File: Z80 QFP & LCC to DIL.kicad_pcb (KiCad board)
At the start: 2 copper layers, 25.4 x 101.6 mm, 3 parts, among them IC1 Z80CPU-LCC, IC2 Z80CPU-LQFP, IC3 Z80CPU-DIP

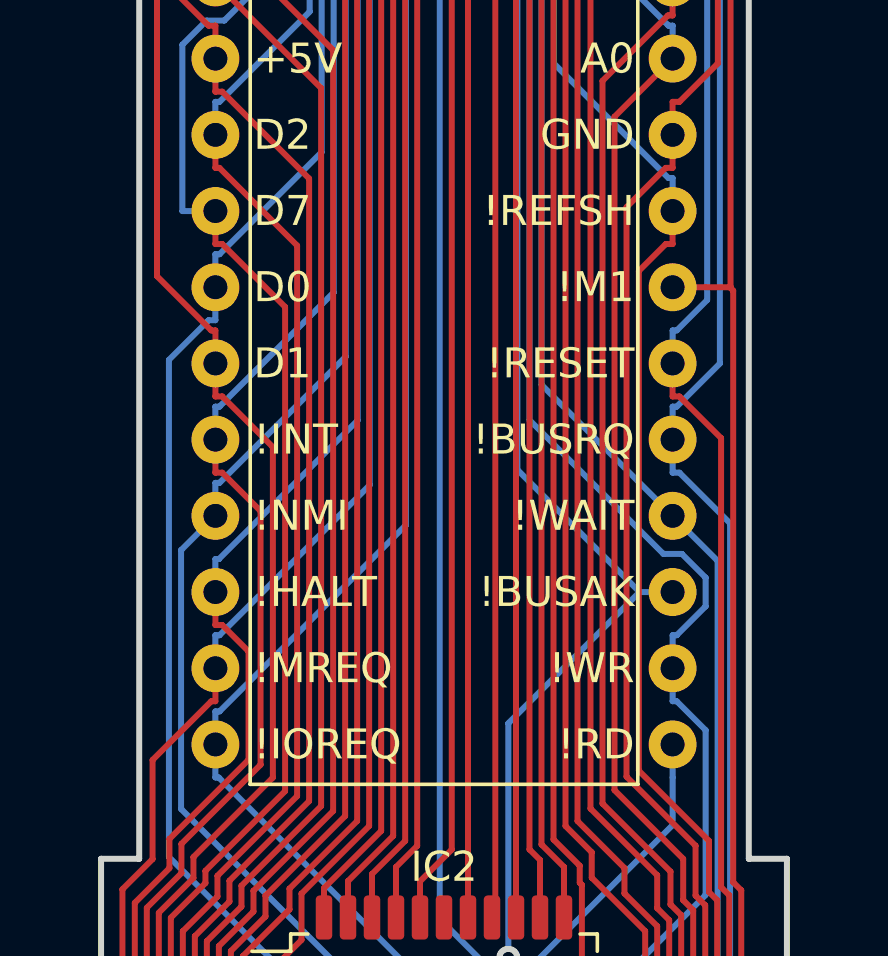
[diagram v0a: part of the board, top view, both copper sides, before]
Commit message: Change text for inveted logic pins from ! to ~{}
Signed-off-by: John Bradley <flypie@rocketmail.com>
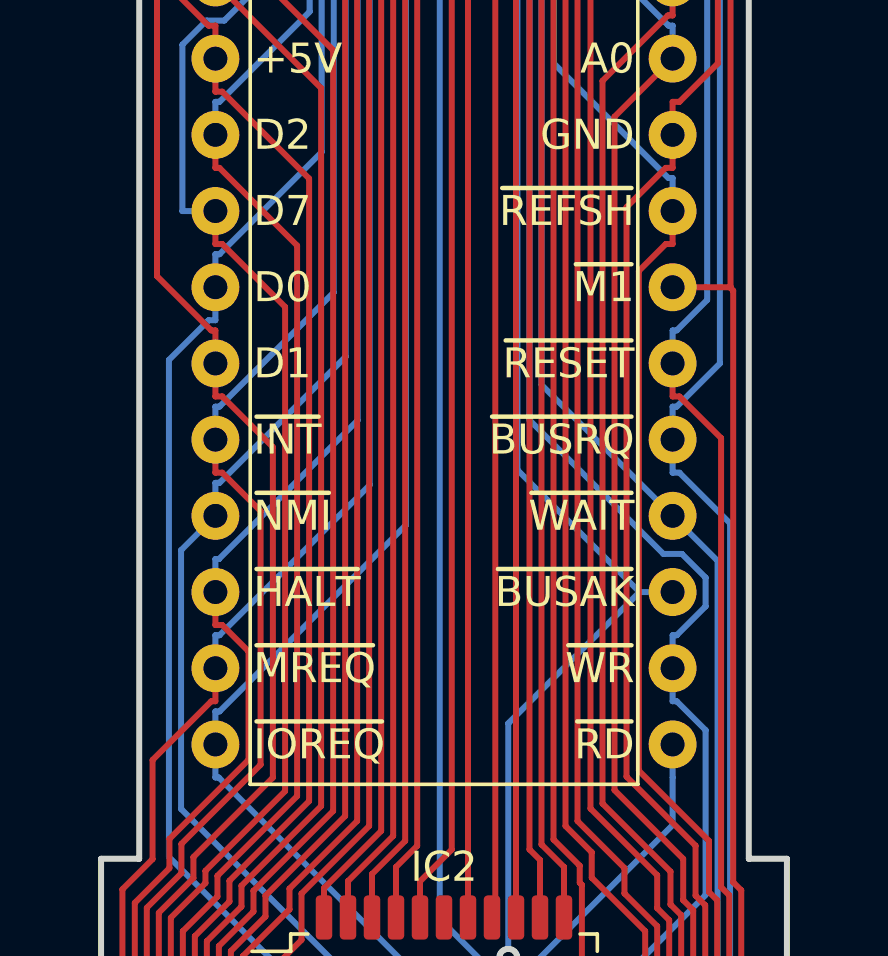
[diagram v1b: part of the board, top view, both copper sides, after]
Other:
- board text added: "~{BUSAK}"
- board text added: "~{BUSRQ}"
- board text added: "~{HALT}"
- board text added: "~{INT}"
- board text added: "~{IOREQ}"
- board text added: "~{M1}"
- board text added: "~{MREQ}"
- board text added: "~{NMI}"
- board text added: "~{RD}"
- board text added: "~{REFSH}"
- board text added: "~{RESET}"
- board text added: "~{WAIT}"
- board text added: "~{WR}"
- board text removed: "!BUSAK"
- board text removed: "!BUSRQ"
- board text removed: "!HALT"
- board text removed: "!INT"
- board text removed: "!IOREQ"
- board text removed: "!M1"
- board text removed: "!MREQ"
- board text removed: "!NMI"
- board text removed: "!RD"
- board text removed: "!REFSH"
- board text removed: "!RESET"
- board text removed: "!WAIT"
- board text removed: "!WR"
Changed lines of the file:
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@@
     (effects (font (size 1 1) (thickness 0.15)) (justify left))
   )
-  (gr_text "!WAIT" (at 147.32 135.89) (layer "F.SilkS")
+  (gr_text "~{WAIT}" (at 147.32 135.89) (layer "F.SilkS")
     (effects (font (size 1 1) (thickness 0.15)) (justify right))
   )
-  (gr_text "!BUSRQ" (at 147.32 133.35) (layer "F.SilkS")
+  (gr_text "~{BUSRQ}" (at 147.32 133.35) (layer "F.SilkS")
     (effects (font (size 1 1) (thickness 0.15)) (justify right))
   )
-  (gr_text "!MREQ" (at 134.62 140.97) (layer "F.SilkS")
+  (gr_text "~{MREQ}" (at 134.62 140.97) (layer "F.SilkS")
     (effects (font (size 1 1) (thickness 0.15)) (justify left))
   )
@@
     (effects (font (size 1 1) (thickness 0.15)) (justify right))
   )
-  (gr_text "!RESET" (at 147.32 130.81) (layer "F.SilkS")
+  (gr_text "~{RESET}" (at 147.32 130.81) (layer "F.SilkS")
     (effects (font (size 1 1) (thickness 0.15)) (justify right))
   )
-  (gr_text "!M1" (at 147.32 128.27) (layer "F.SilkS")
+  (gr_text "~{M1}" (at 147.32 128.27) (layer "F.SilkS")
     (effects (font (size 1 1) (thickness 0.15)) (justify right))
   )
@@
     (effects (font (size 1 1) (thickness 0.15)) (justify left))
   )
-  (gr_text "!REFSH" (at 147.32 125.73) (layer "F.SilkS")
+  (gr_text "~{REFSH}" (at 147.32 125.73) (layer "F.SilkS")
     (effects (font (size 1 1) (thickness 0.15)) (justify right))
   )
@@
     (effects (font (size 1 1) (thickness 0.15)) (justify left))
   )
-  (gr_text "!INT" (at 134.62 133.35) (layer "F.SilkS")
+  (gr_text "~{INT}" (at 134.62 133.35) (layer "F.SilkS")
     (effects (font (size 1 1) (thickness 0.15)) (justify left))
   )
@@
     (effects (font (size 1 1) (thickness 0.15)) (justify right))
   )
-  (gr_text "!BUSAK" (at 147.32 138.43) (layer "F.SilkS")
+  (gr_text "~{BUSAK}" (at 147.32 138.43) (layer "F.SilkS")
     (effects (font (size 1 1) (thickness 0.15)) (justify right))
   )
@@
     (effects (font (size 1 1) (thickness 0.15)) (justify left))
   )
-  (gr_text "!WR" (at 147.32 140.97) (layer "F.SilkS")
+  (gr_text "~{WR}" (at 147.32 140.97) (layer "F.SilkS")
     (effects (font (size 1 1) (thickness 0.15)) (justify right))
   )
@@
     (effects (font (size 1 1) (thickness 0.15)) (justify left))
   )
-  (gr_text "!RD" (at 147.32 143.51) (layer "F.SilkS")
+  (gr_text "~{RD}" (at 147.32 143.51) (layer "F.SilkS")
     (effects (font (size 1 1) (thickness 0.15)) (justify right))
   )
@@
     (effects (font (size 1 1) (thickness 0.15)) (justify left))
   )
-  (gr_text "!IOREQ" (at 134.62 143.51) (layer "F.SilkS")
+  (gr_text "~{IOREQ}" (at 134.62 143.51) (layer "F.SilkS")
     (effects (font (size 1 1) (thickness 0.15)) (justify left))
   )
-  (gr_text "!NMI" (at 134.62 135.89) (layer "F.SilkS")
+  (gr_text "~{NMI}" (at 134.62 135.89) (layer "F.SilkS")
     (effects (font (size 1 1) (thickness 0.15)) (justify left))
   )
-  (gr_text "!HALT" (at 134.62 138.43) (layer "F.SilkS")
+  (gr_text "~{HALT}" (at 134.62 138.43) (layer "F.SilkS")
     (effects (font (size 1 1) (thickness 0.15)) (justify left))
   )
